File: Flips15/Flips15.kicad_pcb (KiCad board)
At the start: 2 copper layers, 100 x 100 mm, 68 parts, among them CN1 UFP2810, U1001 74HC238, U1002 ULN2803A, U1003 74HC238, U1004 TBD62783A, U1101 74HC238, U1102 ULN2803A, U1103 74HC238, U1104 TBD62783A, U701 74HC238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

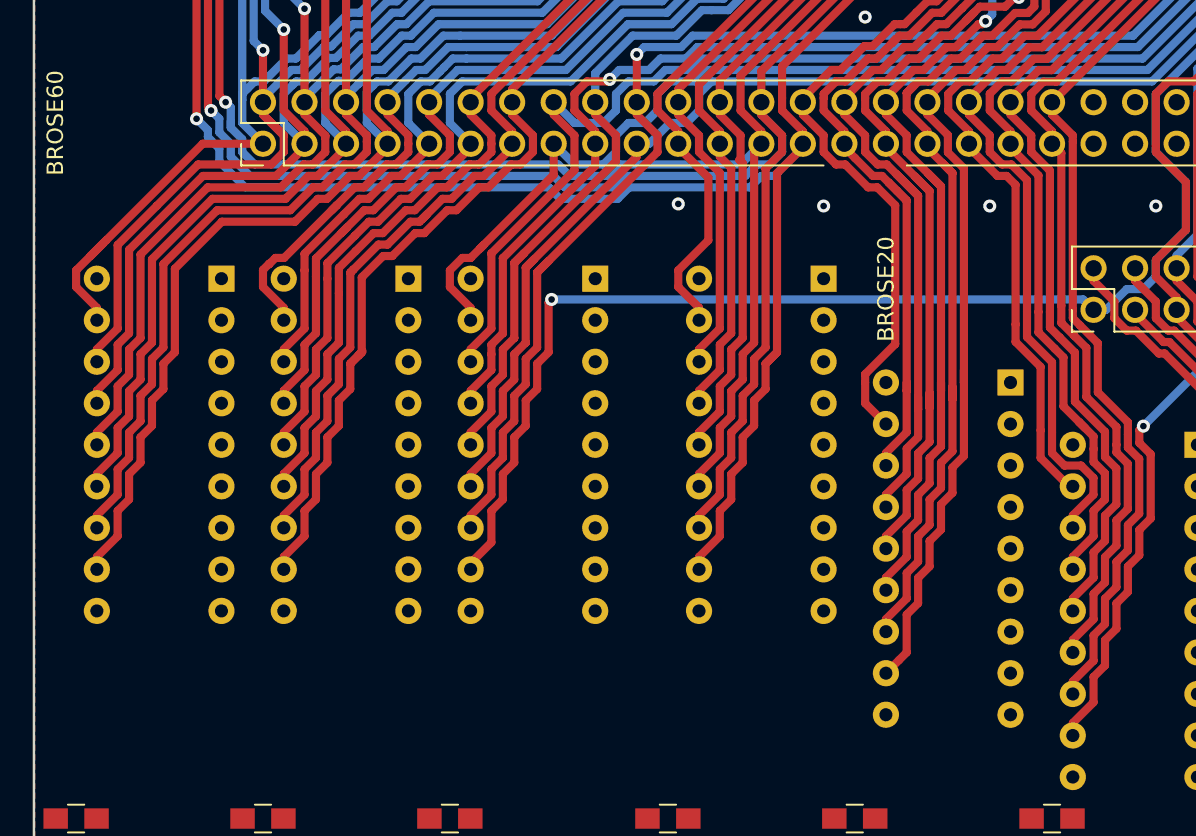
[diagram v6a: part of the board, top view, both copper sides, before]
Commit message: move drivers closer to connector
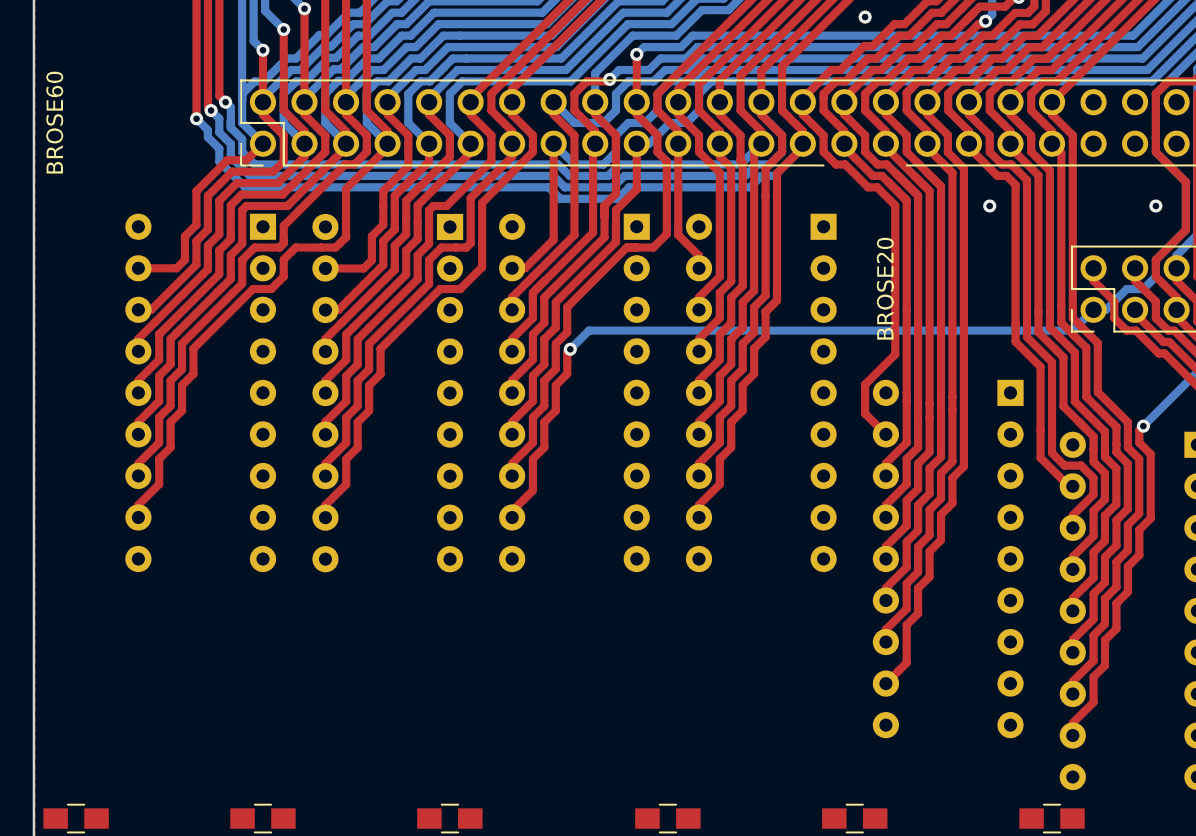
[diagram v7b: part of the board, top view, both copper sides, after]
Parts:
- moved U804 4.07 mm to (64.8, 95.2)
- moved U1004 4.07 mm to (87.6, 95.2)
- moved U904 4.06 mm to (76.2, 95.3)
- moved U802 3.17 mm to (99.1, 95.2)
- moved U902 0.63 mm to (110.5, 105.4)
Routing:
- net /SY21: track 134.9 -> 127.7 mm
- net /SY14: track 85.3 -> 78.8 mm
- net /SY1: track 114.5 -> 108.0 mm
- net /SY6: track 114.9 -> 108.6 mm
- net /SY5: track 129.6 -> 123.9 mm
- net /SY4: track 118.4 -> 112.7 mm
- net /SY10: track 88.4 -> 82.8 mm
- net /SY15: track 108.4 -> 103.0 mm
- net /SY8: track 81.1 -> 75.7 mm
- net /SY13: track 98.9 -> 93.5 mm
- net /SY11: track 95.0 -> 89.8 mm
- net /SY3: track 118.1 -> 112.9 mm
- net /SY12: track 82.3 -> 77.2 mm
- net /SY2: track 115.9 -> 111.0 mm
- net /SY7: track 120.1 -> 115.4 mm
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
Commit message: preparing control wires
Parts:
- moved U803 1.65 mm to (56.9, 137.2)
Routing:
- net /UnitY/Group3/YL0: track 28.2 -> 99.0 mm
- net /UnitY/Group2/YL0: track 0.00 -> 28.2 mm
- net /UnitY/Group1/YL0: track 0.00 -> 28.2 mm
- net /UnitY/Group0/YL0: track 0.00 -> 28.2 mm
- net /UnitY/Group1/YL1: track 0.00 -> 25.2 mm
- net /UnitY/Group0/YL1: track 0.00 -> 25.2 mm
- net /UnitY/Group2/YL1: track 0.00 -> 25.2 mm
- net /UnitY/Group2/YH1: track 0.00 -> 25.2 mm
- net /UnitY/Group1/YL2: track 0.00 -> 22.0 mm
- net /UnitY/Group1/YH2: track 0.00 -> 22.0 mm
- net /UnitY/Group0/YL2: track 0.00 -> 22.0 mm
- net /UnitY/Group0/YH2: track 0.00 -> 22.0 mm
- net /UnitY/Group2/YH2: track 0.00 -> 22.0 mm
- net /UnitY/Group2/YL2: track 0.00 -> 22.0 mm
- net /SY7: track 115.4 -> 136.2 mm
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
